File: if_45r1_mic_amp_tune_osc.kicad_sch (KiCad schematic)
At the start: 0 parts

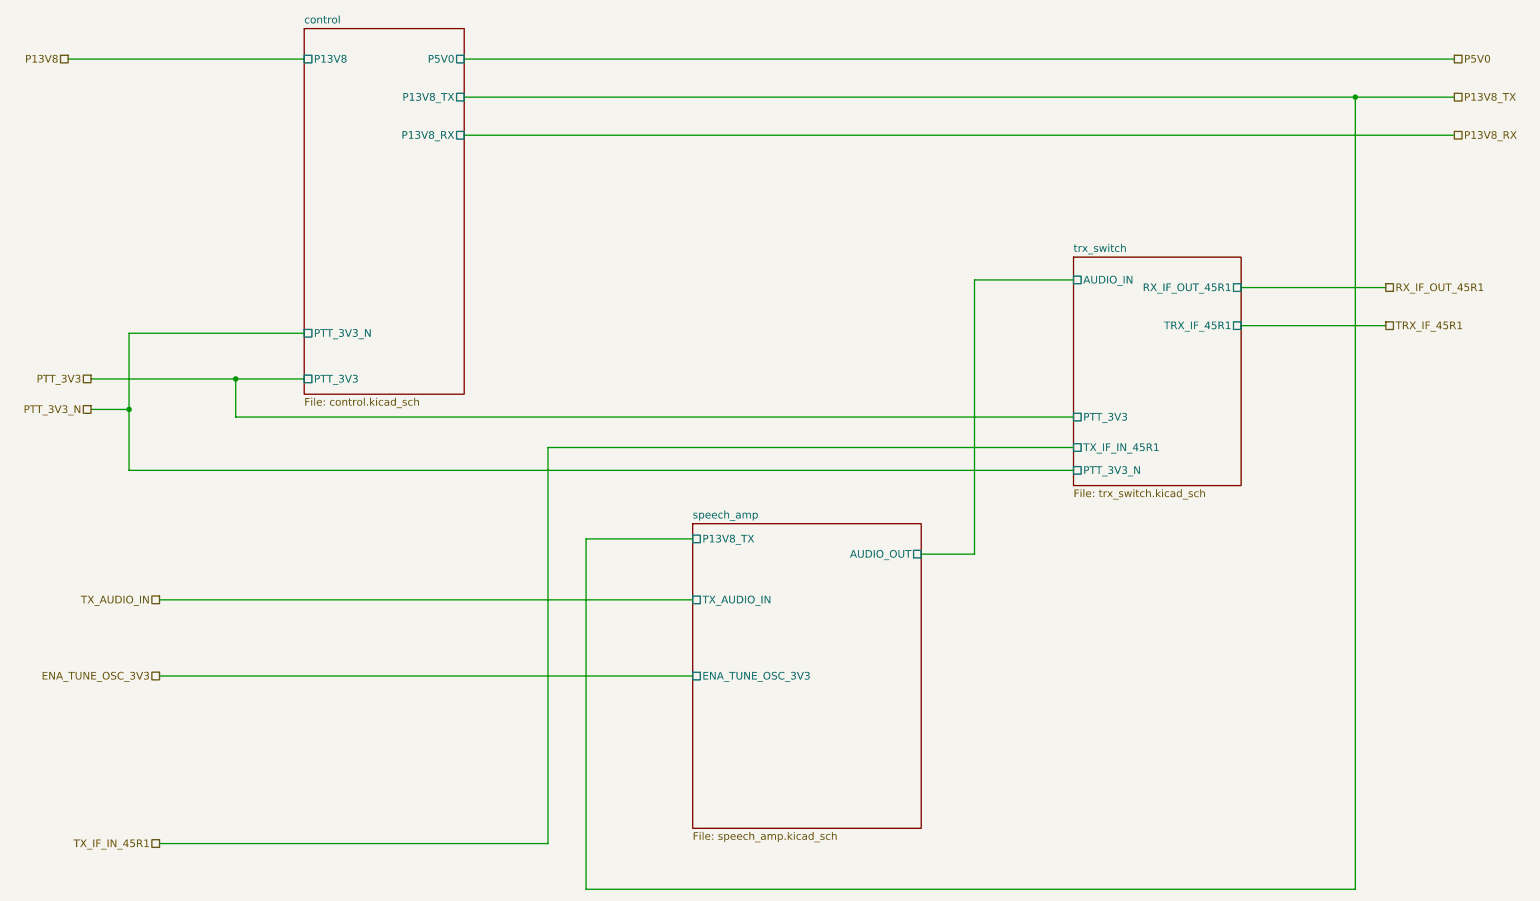
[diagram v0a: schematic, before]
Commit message: trx_mobo_concept_2_B. Change design to use a dedicated 8V supply for the 2SC3357 parts. Add S-Meter connector. Change mic connector to 3 pins and add 8V sopower supply to pin 3.
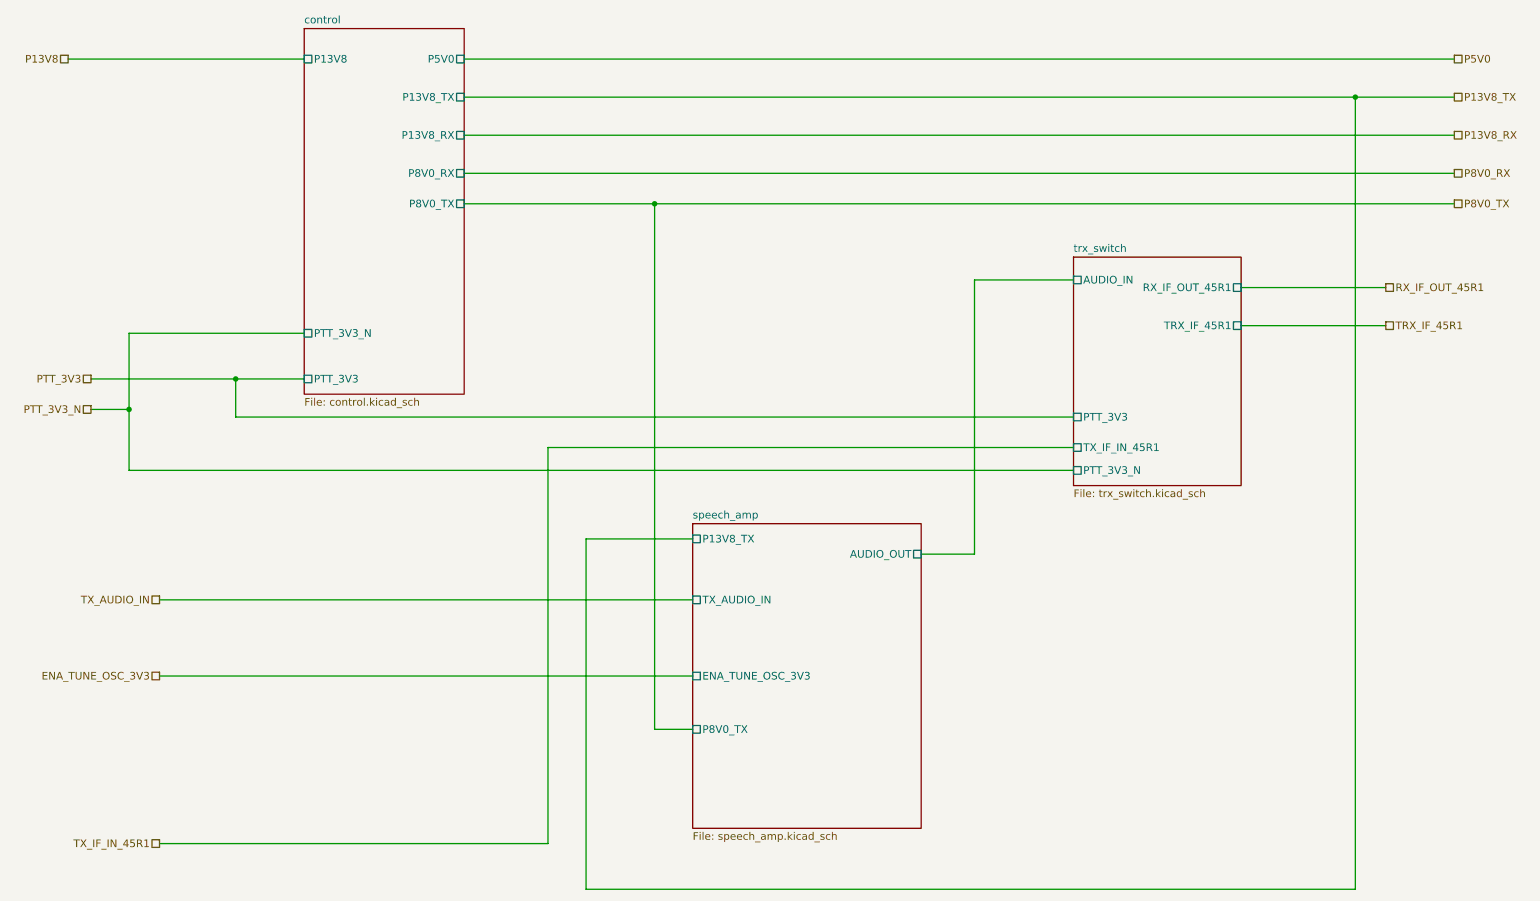
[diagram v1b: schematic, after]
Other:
- sheet control ports: added P8V0_RX, P8V0_TX; removed none
- sheet speech_amp ports: added P8V0_TX; removed none
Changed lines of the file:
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@@
   (paper "A4")
   (title_block
-    (rev "X1")
+    (rev "B")
     (company "WA6ZFT")
   )
+  (junction (at 120.65 48.26) (diameter 0) (color 0 0 0 0)
+  )
   (junction (at 237.49 30.48) (diameter 0) (color 0 0 0 0)
   )
@@
     (stroke (width 0) (type default) (color 0 0 0 0))
   )
+  (wire (pts (xy 120.65 48.26) (xy 254 48.26))
+    (stroke (width 0) (type default) (color 0 0 0 0))
+  )
   (wire (pts (xy 102.87 88.9) (xy 190.5 88.9))
     (stroke (width 0) (type default) (color 0 0 0 0))
@@
     (stroke (width 0) (type default) (color 0 0 0 0))
   )
+  (wire (pts (xy 88.9 43.18) (xy 254 43.18))
+    (stroke (width 0) (type default) (color 0 0 0 0))
+  )
   (wire (pts (xy 62.23 69.85) (xy 33.02 69.85))
     (stroke (width 0) (type default) (color 0 0 0 0))
@@
     (stroke (width 0) (type default) (color 0 0 0 0))
   )
+  (wire (pts (xy 88.9 48.26) (xy 120.65 48.26))
+    (stroke (width 0) (type default) (color 0 0 0 0))
+  )
   (wire (pts (xy 38.1 127) (xy 127 127))
     (stroke (width 0) (type default) (color 0 0 0 0))
@@
     (stroke (width 0) (type default) (color 0 0 0 0))
   )
+  (wire (pts (xy 120.65 48.26) (xy 120.65 135.89))
+    (stroke (width 0) (type default) (color 0 0 0 0))
+  )
   (wire (pts (xy 190.5 83.82) (xy 50.8 83.82))
     (stroke (width 0) (type default) (color 0 0 0 0))
@@
     (stroke (width 0) (type default) (color 0 0 0 0))
   )
+  (wire (pts (xy 127 135.89) (xy 120.65 135.89))
+    (stroke (width 0) (type default) (color 0 0 0 0))
+  )
   (wire (pts (xy 218.44 62.23) (xy 242.57 62.23))
     (stroke (width 0) (type default) (color 0 0 0 0))
@@
     (effects (font (size 1.27 1.27)) (justify left))
   )
+  (hierarchical_label "P8V0_RX" (shape passive) (at 254 43.18 0)
+    (effects (font (size 1.27 1.27)) (justify left))
+  )
   (hierarchical_label "P13V8" (shape passive) (at 22.86 24.13 180)
     (effects (font (size 1.27 1.27)) (justify right))
@@
   (hierarchical_label "TX_AUDIO_IN" (shape passive) (at 38.1 114.3 180)
     (effects (font (size 1.27 1.27)) (justify right))
+  )
+  (hierarchical_label "P8V0_TX" (shape passive) (at 254 48.26 0)
+    (effects (font (size 1.27 1.27)) (justify left))
   )
   (hierarchical_label "TX_IF_IN_45R1" (shape passive) (at 38.1 154.94 180)
@@
       (effects (font (size 1.27 1.27)) (justify left))
     )
+    (pin "P8V0_TX" passive (at 127 135.89 180)
+      (effects (font (size 1.27 1.27)) (justify left))
+    )
   )
   (sheet (at 190.5 57.15) (size 27.94 38.1) (fields_autoplaced)
@@
       (effects (font (size 1.27 1.27)) (justify left))
     )
-  )
+    (pin "P8V0_RX" passive (at 88.9 43.18 0)
+      (effects (font (size 1.27 1.27)) (justify right))
+    )
+    (pin "P8V0_TX" passive (at 88.9 48.26 0)
+      (effects (font (size 1.27 1.27)) (justify right))
+    )
+  )
